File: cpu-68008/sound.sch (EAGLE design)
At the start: 62 parts, among them IC101 GAL22V10D, IC102 74HCT175N, IC201 YM3812, IC202 YM3014B, IC203 AY-3-8910, IC301 TL062, IC302 TL062, IC401 74HCT14N, IC402 SCC2691, J301 RCALOCK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

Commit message: added /DS to GALs on all peripherals and backplane began work on TMS9918 video card
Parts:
- added LED401, LED402: (no value), led:LEDCHIPLED_1206
- added R405: 220R, rcl:R-EU_R2012
- added R406: 4k7, rcl:R-EU_R2012
- R403: value 220R -> 3k; MOUSER 652-CR0805FX-2200ELF -> 652-CR0805JW-302ELF
- R404: value 4k7 -> 3k; MOUSER 652-CR0805FX-4701ELF -> 652-CR0805JW-302ELF
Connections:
- removed net !RESET: IC101.IO18, IC201.!RESET, IC203.!RESET, IC401C.I
- new net N$3: LED401.A, R403.2
- new net N$8: LED402.A, R404.2
- net !MIDI_IRQ: now also R406.1; no longer R404.1
- net !SLOT_DS: now also IC101.IN5
- net !SLOT_RESET: now also IC201.!RESET, IC203.!RESET, IC401C.I; no longer IC101.IN5
- net +5V: now also R403.1, R404.1, R405.2, R406.2; no longer R403.2, R404.2
- net MIDI_RX: now also LED401.C
- net MIDI_TX: now also LED402.C
- net N$17: now also R405.1; no longer R403.1
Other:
- moved on the sheet: R403, R404

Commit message: finished schematic for tms9918 board, started routing
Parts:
- C303: MOUSER 710-860020273009 -> 710-860020373010
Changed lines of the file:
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@@
 </pinmapping>
 </spice>
-<attribute name="MOUSER" value="710-860020273009"/>
+<attribute name="MOUSER" value="710-860020373010"/>
 </part>
 <part name="R309" library="rcl" library_urn="urn:adsk.eagle:library:334" deviceset="R-EU_" device="R2012" package3d_urn="urn:adsk.eagle:package:23543/2" value="4k7">

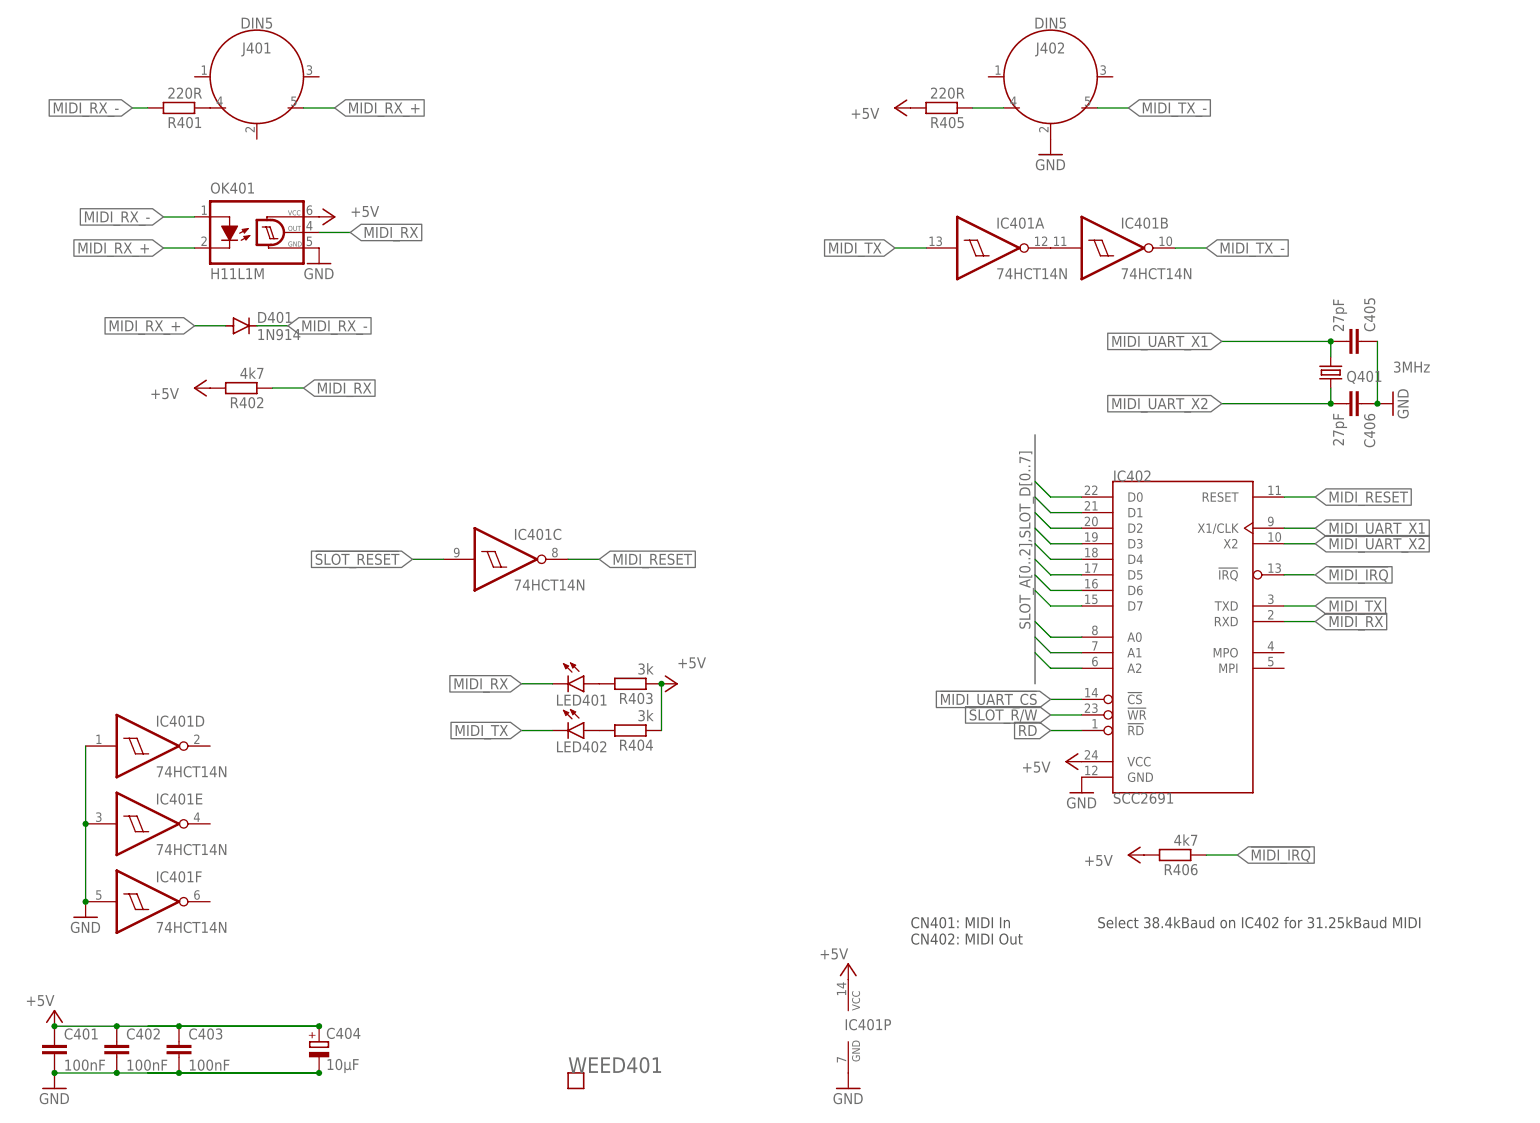
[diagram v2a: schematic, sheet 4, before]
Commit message: minor revisions on mouser parts
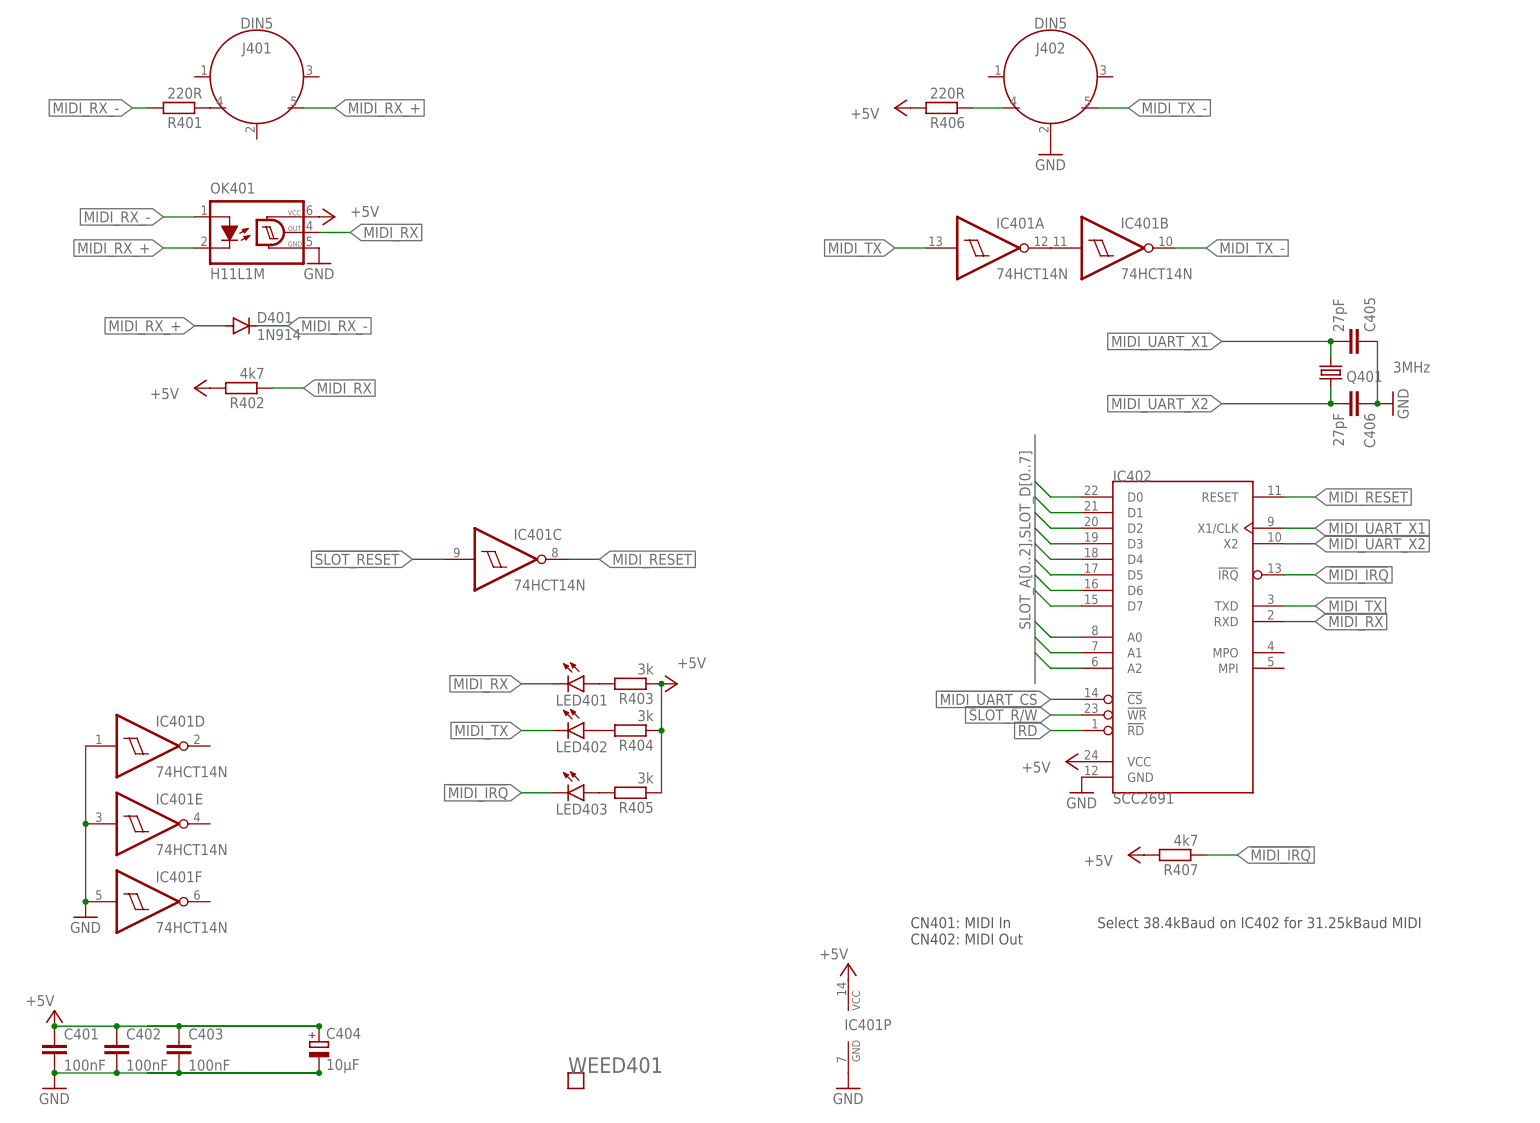
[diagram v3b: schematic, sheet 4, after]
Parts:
- added LED201, LED403: (no value), led:LEDCHIPLED_1206
- added R201: 3k, rcl:R-EU_R2012
- added R407: 4k7, rcl:R-EU_R2012
- J401, J402: MOUSER (none) -> 806-KCDX-5S-N
- R405: value 220R -> 3k; MOUSER 652-CR0805FX-2200ELF -> 652-CR0805JW-302ELF
- R406: value 4k7 -> 220R; MOUSER 652-CR0805FX-4701ELF -> 652-CR0805FX-2200ELF
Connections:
- new net N$18: LED403.A, R405.2
- new net N$9: LED201.A, R201.2
- net !MIDI_IRQ: now also LED403.C, R407.1; no longer R406.1
- net !YM_IRQ: now also LED201.C
- net +5V: now also R201.1, R405.1, R407.2; no longer R405.2
- net N$17: now also R406.1; no longer R405.1
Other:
- moved on the sheet: R405, R406
